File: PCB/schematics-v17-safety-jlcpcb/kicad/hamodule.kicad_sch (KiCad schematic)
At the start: 94 parts, among them J1 Conn_01x02_Male, J10 2604-1104, J11 ESP Relays, J12 2604-1104, J13 EspSense, J2 2604-1102, J3 GND|5V, J4 GND|3.3V, J5 Jumper, J6 Conn_01x02_Male, J7 Current Jumper, J8 USB_C_Receptacle_USB2.0, J9 DoNotCon, K1 PCN-105D, K2 PCN-105D, K3 PCN-105D, K4 PCN-105D, Q1 SS8050-SMD, Q2 SS8050, SW1 EN, SW2 IO0, U1 LD1117AV33_TO220, U2 ESP32-WROOM-32E, U3 CP2102N-A01-GQFN28, U4 ULN2003A, U5 LDA210-PDIP, U6 LDA210-PDIP, U7 SHT4x

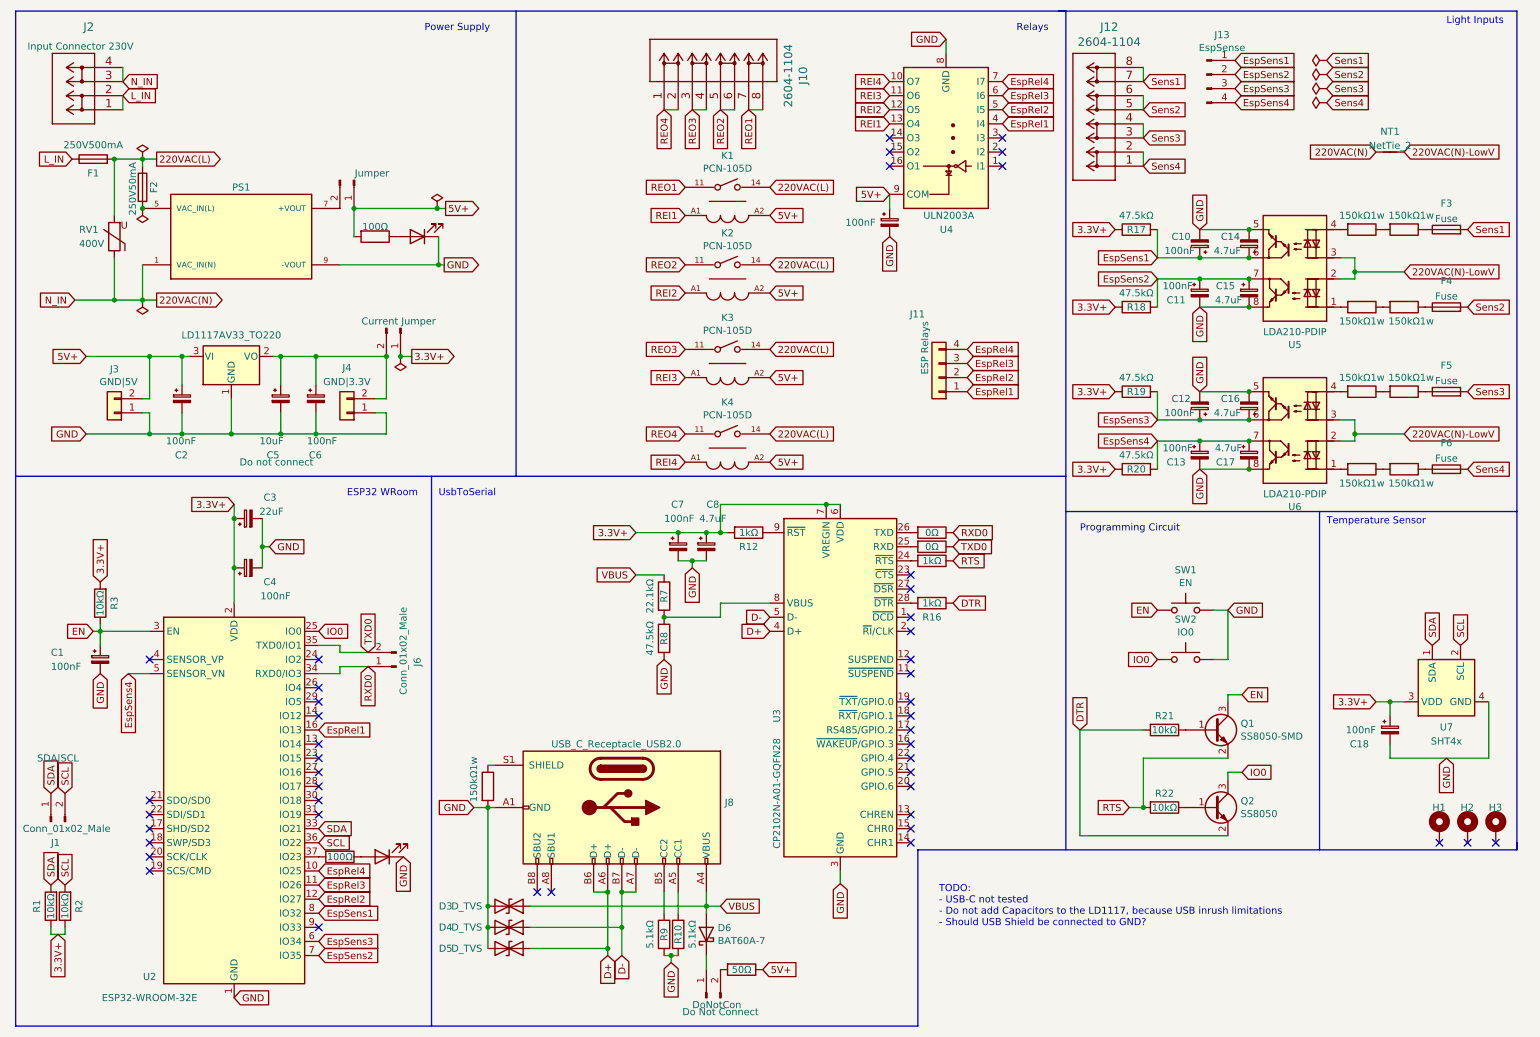
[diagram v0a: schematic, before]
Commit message: [BUG] v17 - R11 lowers V too much and ESP cannot be programmed. Replacing by 0Ohms to not to change layout (removed in future versions)
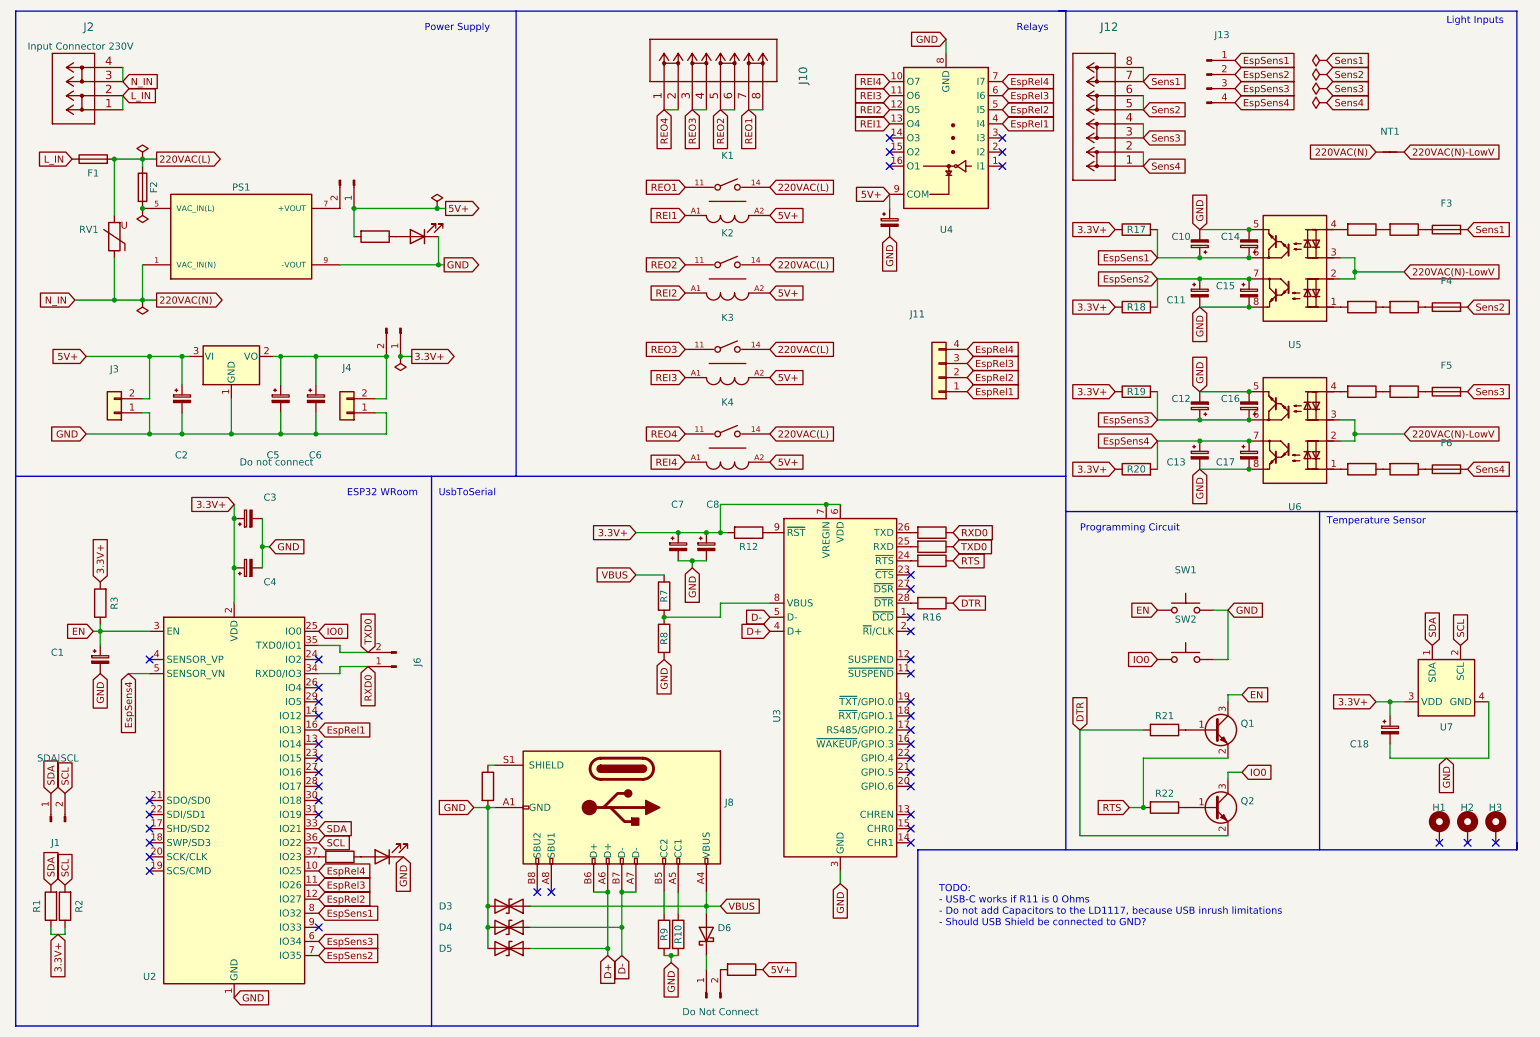
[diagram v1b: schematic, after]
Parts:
- C1, C10, C11, C12, C13, C18, C2, C4, C6, C7, C9: value 100nF -> (none); footprint Capacitor_SMD:C_0603_1608Metric_Pad1.08x0.95mm_HandSolder -> (none)
- C14, C16, C17: value 4.7uF -> (none); footprint Capacitor_SMD:C_1206_3216Metric_Pad1.33x1.80mm_HandSolder -> (none)
- C15: footprint Capacitor_SMD:C_1206_3216Metric_Pad1.33x1.80mm_HandSolder -> (none)
- C3: value 22uF -> (none); footprint Capacitor_SMD:C_0603_1608Metric_Pad1.08x0.95mm_HandSolder -> (none)
- C5: value 10uF -> (none); footprint Capacitor_THT:CP_Radial_D6.3mm_P2.50mm -> (none)
- C8: value 4.7uF -> (none); footprint Capacitor_SMD:C_0603_1608Metric_Pad1.08x0.95mm_HandSolder -> (none)
- D1, D2: value LED -> (none); footprint LED_SMD:LED_0805_2012Metric_Pad1.15x1.40mm_HandSolder -> (none)
- D3, D4, D5: value D_TVS -> (none); footprint Diode_SMD:D_SOD-523 -> (none)
- D6: value BAT60A-7 -> (none); footprint Diode_SMD:D_SOD-323 -> (none)
- F1: value 250V500mA -> (none); footprint Fuse:Fuseholder_TR5_Littelfuse_No560_No460 -> (none)
- F2: value 250V50mA -> (none); footprint Fuse:Fuseholder_TR5_Littelfuse_No560_No460 -> (none)
- F3, F4, F5, F6: value Fuse -> (none); footprint RST-80-AMMO:FUSE_RST-1-BULK -> (none)
- H1, H2, H3: value MountingHole_Pad -> (none); footprint MountingHole:MountingHole_3.2mm_M3_ISO14580_Pad -> (none)
- J1, J6: value Conn_01x02_Male -> (none); footprint Connector_PinHeader_2.54mm:PinHeader_1x02_P2.54mm_Vertical -> (none)
- J10, J12: value 2604-1104 -> (none); footprint wago-2604-1104:big_pads_2604-1104 -> (none)
- J11: value ESP Relays -> (none); footprint Connector_JST:JST_XH_B4B-XH-A_1x04_P2.50mm_Vertical -> (none)
- J13: value EspSense -> (none); footprint Connector_PinSocket_2.54mm:PinSocket_1x04_P2.54mm_Vertical -> (none)
- J2: value 2604-1102 -> (none); footprint wago-2604-1102:big_pads_2604-1102 -> (none)
- J3: value GND|5V -> (none); footprint Connector_JST:JST_XH_B2B-XH-A_1x02_P2.50mm_Vertical -> (none)
- J4: value GND|3.3V -> (none); footprint Connector_JST:JST_XH_B2B-XH-A_1x02_P2.50mm_Vertical -> (none)
- J5: value Jumper -> (none); footprint Connector_PinHeader_2.54mm:PinHeader_1x02_P2.54mm_Vertical -> (none)
- J7: value Current Jumper -> (none); footprint Connector_PinHeader_2.54mm:PinHeader_1x02_P2.54mm_Vertical -> (none)
- J8: value USB_C_Receptacle_USB2.0 -> (none); footprint Connector_USB:USB_C_Receptacle_HRO_TYPE-C-31-M-12 -> (none)
- J9: value DoNotCon -> (none); footprint Connector_PinHeader_2.54mm:PinHeader_1x02_P2.54mm_Vertical -> (none)
- K1, K2, K3, K4: value PCN-105D -> (none); footprint PCN:bigpads_TE_Connectivity-PCN-124D -> (none)
- NT1: value NetTie_2 -> (none); footprint NetTie:NetTie-2_SMD_Pad2.0mm -> (none)
- PS1: value RAC05-05SK/277 -> (none); footprint rac05-05sk:277 -> (none)
- Q1: value SS8050-SMD -> (none); footprint Package_TO_SOT_SMD:SOT-23 -> (none)
- Q2: value SS8050 -> (none); footprint Package_TO_SOT_SMD:SOT-23 -> (none)
- R1, R2, R21, R22, R3: value 10kΩ -> (none); footprint Resistor_SMD:R_0603_1608Metric_Pad0.98x0.95mm_HandSolder -> (none)
- R10, R9: value 5.1kΩ -> (none); footprint Resistor_SMD:R_0603_1608Metric_Pad0.98x0.95mm_HandSolder -> (none)
- R11: value 50Ω -> (none); footprint Resistor_SMD:R_0805_2012Metric_Pad1.20x1.40mm_HandSolder -> (none); JLCPCB C17738 -> C17477
- R12, R16: value 1kΩ -> (none); footprint Resistor_SMD:R_0603_1608Metric_Pad0.98x0.95mm_HandSolder -> (none)
- R13, R14: value 0Ω -> (none); footprint Resistor_SMD:R_0805_2012Metric_Pad1.20x1.40mm_HandSolder -> (none)
- R15: value 1kΩ -> (none); footprint Resistor_SMD:R_1206_3216Metric_Pad1.30x1.75mm_HandSolder -> (none)
- R17, R18, R19, R20, R8: value 47.5kΩ -> (none); footprint Resistor_SMD:R_0603_1608Metric_Pad0.98x0.95mm_HandSolder -> (none)
- R23, R24, R25, R26, R27, R28, R29, R30, R6: value 150kΩ1w -> (none); footprint Resistor_SMD:R_2512_6332Metric_Pad1.40x3.35mm_HandSolder -> (none)
- R4, R5: value 100Ω -> (none); footprint Resistor_SMD:R_0805_2012Metric_Pad1.20x1.40mm_HandSolder -> (none)
- R7: value 22.1kΩ -> (none); footprint Resistor_SMD:R_0603_1608Metric_Pad0.98x0.95mm_HandSolder -> (none)
- RV1: value 400V -> (none); footprint Varistor:RV_Disc_D12mm_W4.2mm_P7.5mm -> (none)
- SW1: value EN -> (none); footprint Button_Switch_SMD:SW_SPST_SKQG_WithStem -> (none)
- SW2: value IO0 -> (none); footprint Button_Switch_SMD:SW_SPST_SKQG_WithStem -> (none)
- U1: value LD1117AV33_TO220 -> (none); footprint Package_TO_SOT_THT:TO-220-3_Vertical -> (none)
- U2: value ESP32-WROOM-32E -> (none); footprint RF_Module:ESP32-WROOM-32 -> (none)
- U3: value CP2102N-A01-GQFN28 -> (none); footprint Package_DFN_QFN:QFN-28-1EP_5x5mm_P0.5mm_EP3.35x3.35mm -> (none)
- U4: value ULN2003A -> (none); footprint Package_SO:SOIC-16_3.9x9.9mm_P1.27mm -> (none)
- U5, U6: value LDA210-PDIP -> (none); footprint Package_DIP:DIP-8_W7.62mm_Socket_LongPads -> (none)
- U7: value SHT4x -> (none); footprint sht40:XDCR_SHT40-AD1B-R2 -> (none)
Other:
- note added: "TODO: - USB-C works if R11 is 0 Ohms - Do not add Capacitors to the LD1117, because USB inrush limitations - Should USB Shield be connected to GND?"
- note removed: "TODO: - USB-C not tested - Do not add Capacitors to the LD1117, because USB inrush limitations - Should USB Shield be connected to GND?"

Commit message: [V17][BUG] Updating the readme with the latest schematic image, showing the fix of the USB resistor bug
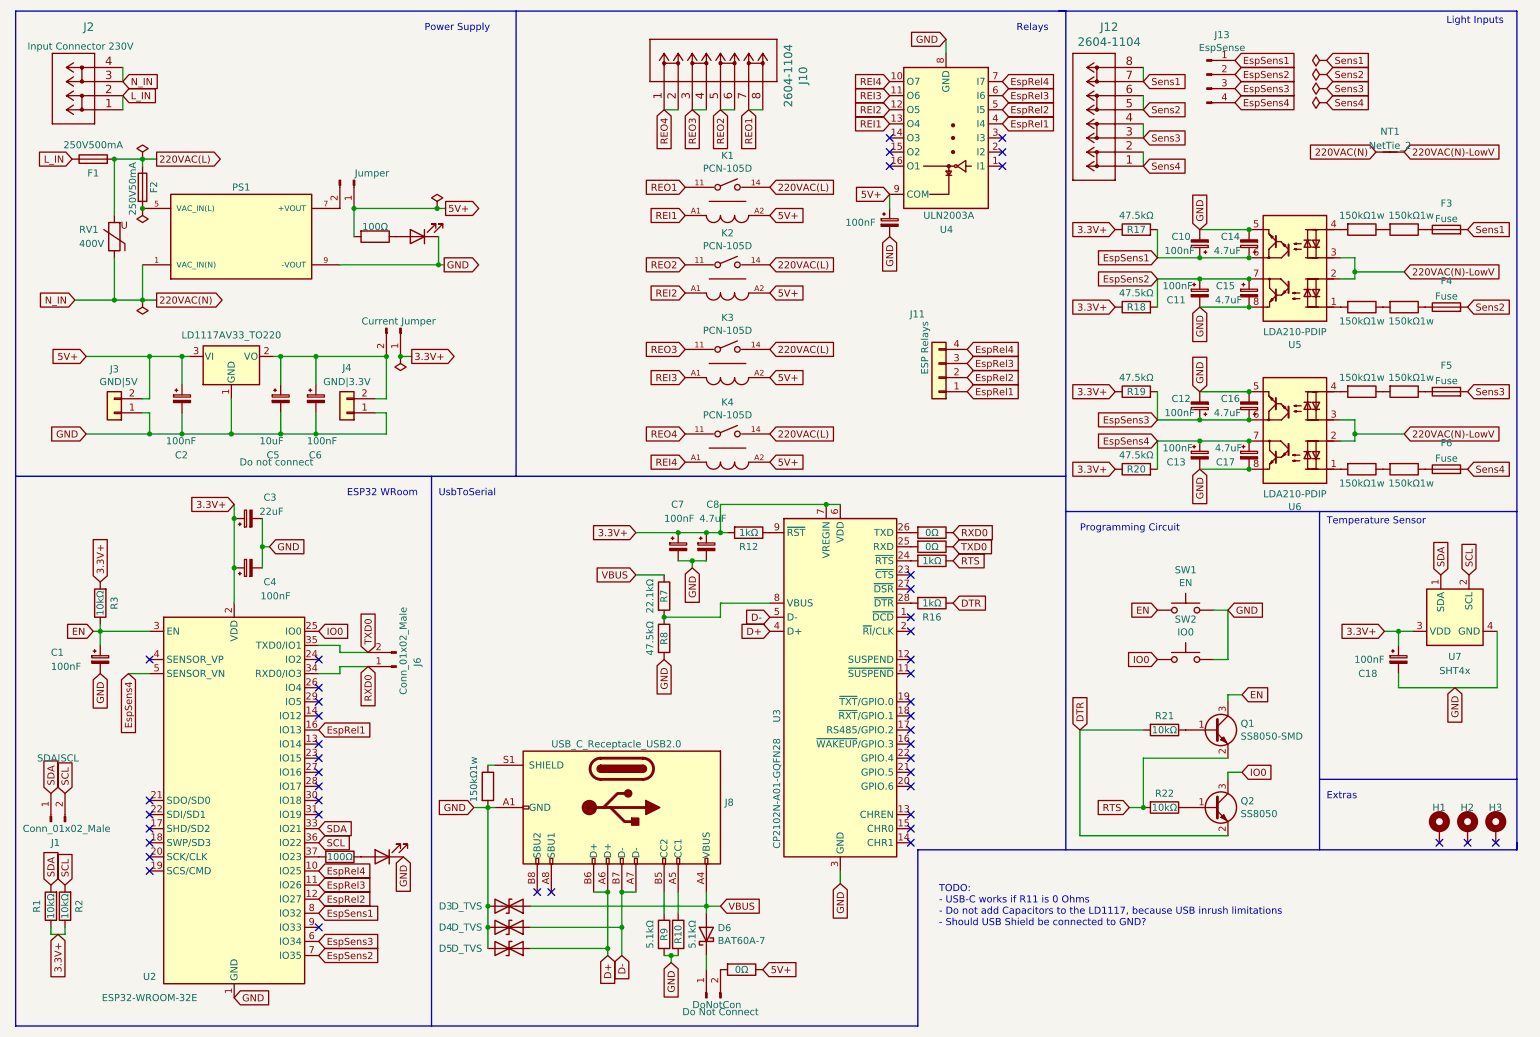
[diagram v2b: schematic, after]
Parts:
- C1, C10, C11, C12, C13, C18, C2, C4, C6, C7, C9: value (none) -> 100nF; footprint (none) -> Capacitor_SMD:C_0603_1608Metric_Pad1.08x0.95mm_HandSolder
- C14, C16, C17: value (none) -> 4.7uF; footprint (none) -> Capacitor_SMD:C_1206_3216Metric_Pad1.33x1.80mm_HandSolder
- C15: footprint (none) -> Capacitor_SMD:C_1206_3216Metric_Pad1.33x1.80mm_HandSolder
- C3: value (none) -> 22uF; footprint (none) -> Capacitor_SMD:C_0603_1608Metric_Pad1.08x0.95mm_HandSolder
- C5: value (none) -> 10uF; footprint (none) -> Capacitor_THT:CP_Radial_D6.3mm_P2.50mm
- C8: value (none) -> 4.7uF; footprint (none) -> Capacitor_SMD:C_0603_1608Metric_Pad1.08x0.95mm_HandSolder
- D1, D2: value (none) -> LED; footprint (none) -> LED_SMD:LED_0805_2012Metric_Pad1.15x1.40mm_HandSolder
- D3, D4, D5: value (none) -> D_TVS; footprint (none) -> Diode_SMD:D_SOD-523
- D6: value (none) -> BAT60A-7; footprint (none) -> Diode_SMD:D_SOD-323
- F1: value (none) -> 250V500mA; footprint (none) -> Fuse:Fuseholder_TR5_Littelfuse_No560_No460
- F2: value (none) -> 250V50mA; footprint (none) -> Fuse:Fuseholder_TR5_Littelfuse_No560_No460
- F3, F4, F5, F6: value (none) -> Fuse; footprint (none) -> RST-80-AMMO:FUSE_RST-1-BULK
- H1, H2, H3: value (none) -> MountingHole_Pad; footprint (none) -> MountingHole:MountingHole_3.2mm_M3_ISO14580_Pad
- J1, J6: value (none) -> Conn_01x02_Male; footprint (none) -> Connector_PinHeader_2.54mm:PinHeader_1x02_P2.54mm_Vertical
- J10, J12: value (none) -> 2604-1104; footprint (none) -> wago-2604-1104:big_pads_2604-1104
- J11: value (none) -> ESP Relays; footprint (none) -> Connector_JST:JST_XH_B4B-XH-A_1x04_P2.50mm_Vertical
- J13: value (none) -> EspSense; footprint (none) -> Connector_PinSocket_2.54mm:PinSocket_1x04_P2.54mm_Vertical
- J2: value (none) -> 2604-1102; footprint (none) -> wago-2604-1102:big_pads_2604-1102
- J3: value (none) -> GND|5V; footprint (none) -> Connector_JST:JST_XH_B2B-XH-A_1x02_P2.50mm_Vertical
- J4: value (none) -> GND|3.3V; footprint (none) -> Connector_JST:JST_XH_B2B-XH-A_1x02_P2.50mm_Vertical
- J5: value (none) -> Jumper; footprint (none) -> Connector_PinHeader_2.54mm:PinHeader_1x02_P2.54mm_Vertical
- J7: value (none) -> Current Jumper; footprint (none) -> Connector_PinHeader_2.54mm:PinHeader_1x02_P2.54mm_Vertical
- J8: value (none) -> USB_C_Receptacle_USB2.0; footprint (none) -> Connector_USB:USB_C_Receptacle_HRO_TYPE-C-31-M-12
- J9: value (none) -> DoNotCon; footprint (none) -> Connector_PinHeader_2.54mm:PinHeader_1x02_P2.54mm_Vertical
- K1, K2, K3, K4: value (none) -> PCN-105D; footprint (none) -> PCN:bigpads_TE_Connectivity-PCN-124D
- NT1: value (none) -> NetTie_2; footprint (none) -> NetTie:NetTie-2_SMD_Pad2.0mm
- PS1: value (none) -> RAC05-05SK/277; footprint (none) -> rac05-05sk:277
- Q1: value (none) -> SS8050-SMD; footprint (none) -> Package_TO_SOT_SMD:SOT-23
- Q2: value (none) -> SS8050; footprint (none) -> Package_TO_SOT_SMD:SOT-23
- R1, R2, R21, R22, R3: value (none) -> 10kΩ; footprint (none) -> Resistor_SMD:R_0603_1608Metric_Pad0.98x0.95mm_HandSolder
- R10, R9: value (none) -> 5.1kΩ; footprint (none) -> Resistor_SMD:R_0603_1608Metric_Pad0.98x0.95mm_HandSolder
- R11, R13, R14: value (none) -> 0Ω; footprint (none) -> Resistor_SMD:R_0805_2012Metric_Pad1.20x1.40mm_HandSolder
- R12, R16: value (none) -> 1kΩ; footprint (none) -> Resistor_SMD:R_0603_1608Metric_Pad0.98x0.95mm_HandSolder
- R15: value (none) -> 1kΩ; footprint (none) -> Resistor_SMD:R_1206_3216Metric_Pad1.30x1.75mm_HandSolder
- R17, R18, R19, R20, R8: value (none) -> 47.5kΩ; footprint (none) -> Resistor_SMD:R_0603_1608Metric_Pad0.98x0.95mm_HandSolder
- R23, R24, R25, R26, R27, R28, R29, R30, R6: value (none) -> 150kΩ1w; footprint (none) -> Resistor_SMD:R_2512_6332Metric_Pad1.40x3.35mm_HandSolder
- R4, R5: value (none) -> 100Ω; footprint (none) -> Resistor_SMD:R_0805_2012Metric_Pad1.20x1.40mm_HandSolder
- R7: value (none) -> 22.1kΩ; footprint (none) -> Resistor_SMD:R_0603_1608Metric_Pad0.98x0.95mm_HandSolder
- RV1: value (none) -> 400V; footprint (none) -> Varistor:RV_Disc_D12mm_W4.2mm_P7.5mm
- SW1: value (none) -> EN; footprint (none) -> Button_Switch_SMD:SW_SPST_SKQG_WithStem
- SW2: value (none) -> IO0; footprint (none) -> Button_Switch_SMD:SW_SPST_SKQG_WithStem
- U1: value (none) -> LD1117AV33_TO220; footprint (none) -> Package_TO_SOT_THT:TO-220-3_Vertical
- U2: value (none) -> ESP32-WROOM-32E; footprint (none) -> RF_Module:ESP32-WROOM-32
- U3: value (none) -> CP2102N-A01-GQFN28; footprint (none) -> Package_DFN_QFN:QFN-28-1EP_5x5mm_P0.5mm_EP3.35x3.35mm
- U4: value (none) -> ULN2003A; footprint (none) -> Package_SO:SOIC-16_3.9x9.9mm_P1.27mm
- U5, U6: value (none) -> LDA210-PDIP; footprint (none) -> Package_DIP:DIP-8_W7.62mm_Socket_LongPads
- U7: value (none) -> SHT4x; footprint (none) -> sht40:XDCR_SHT40-AD1B-R2
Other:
- note added: "Extras"
- moved on the sheet: C18, U7
